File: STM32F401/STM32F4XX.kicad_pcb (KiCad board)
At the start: 2 copper layers, 61 x 68.6 mm, 34 parts, among them J1 DEBUG UART, J2 Conn_02x16_Counter_Clockwise, J3 USB_B_Mini, J4 Conn_02x16_Counter_Clockwise, J5 JTAG SWDIO SWCLK, SW1 ~RESET, U1 STM32F401RCT6, U2 LM1117-3.3, Y1 8MHz

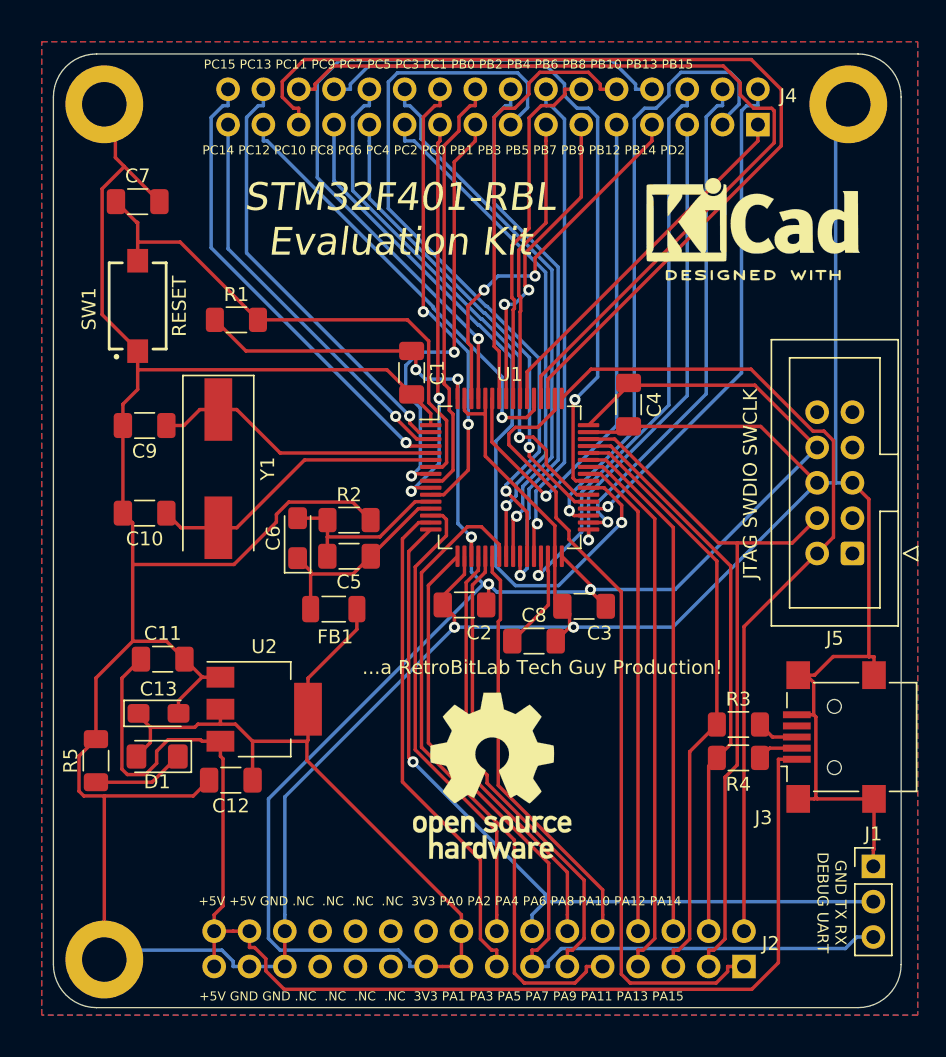
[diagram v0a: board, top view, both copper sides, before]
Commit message: V0.4 USB+ and USB- bug, BOY UART
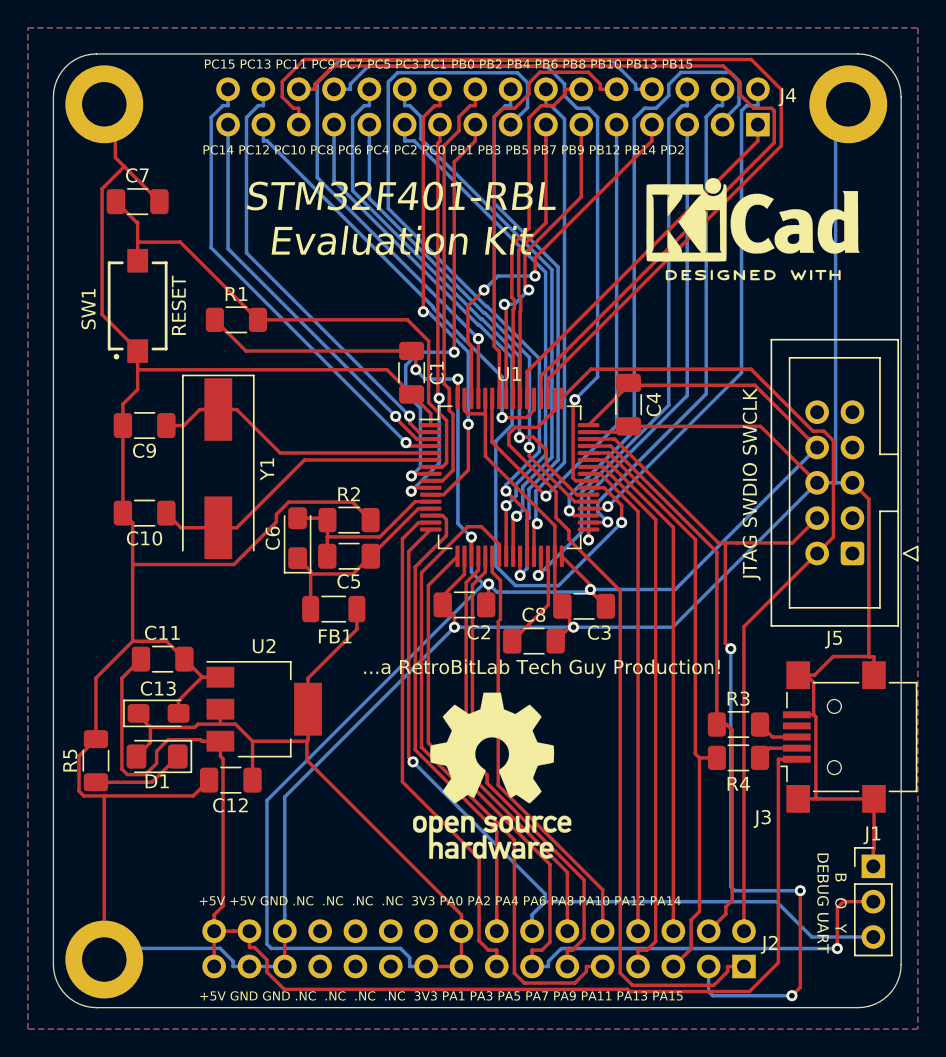
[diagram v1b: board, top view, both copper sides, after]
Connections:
- J1 pad 2: A2 -> A3
- J1 pad 3: A3 -> A2
- R3 pad 1: A11 -> A12
- R4 pad 1: A12 -> A11
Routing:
- net A13: track 51.8 -> 66.0 mm, vias 0 -> 3
- net A3: track 60.3 -> 63.4 mm, vias 0 -> 1
- net A2: track 57.6 -> 58.6 mm
- net +3V3: track 191.0 -> 191.6 mm
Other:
- board text added: "B O Y DEBUG UART"
- board text removed: "GND TX RX DEBUG UART"

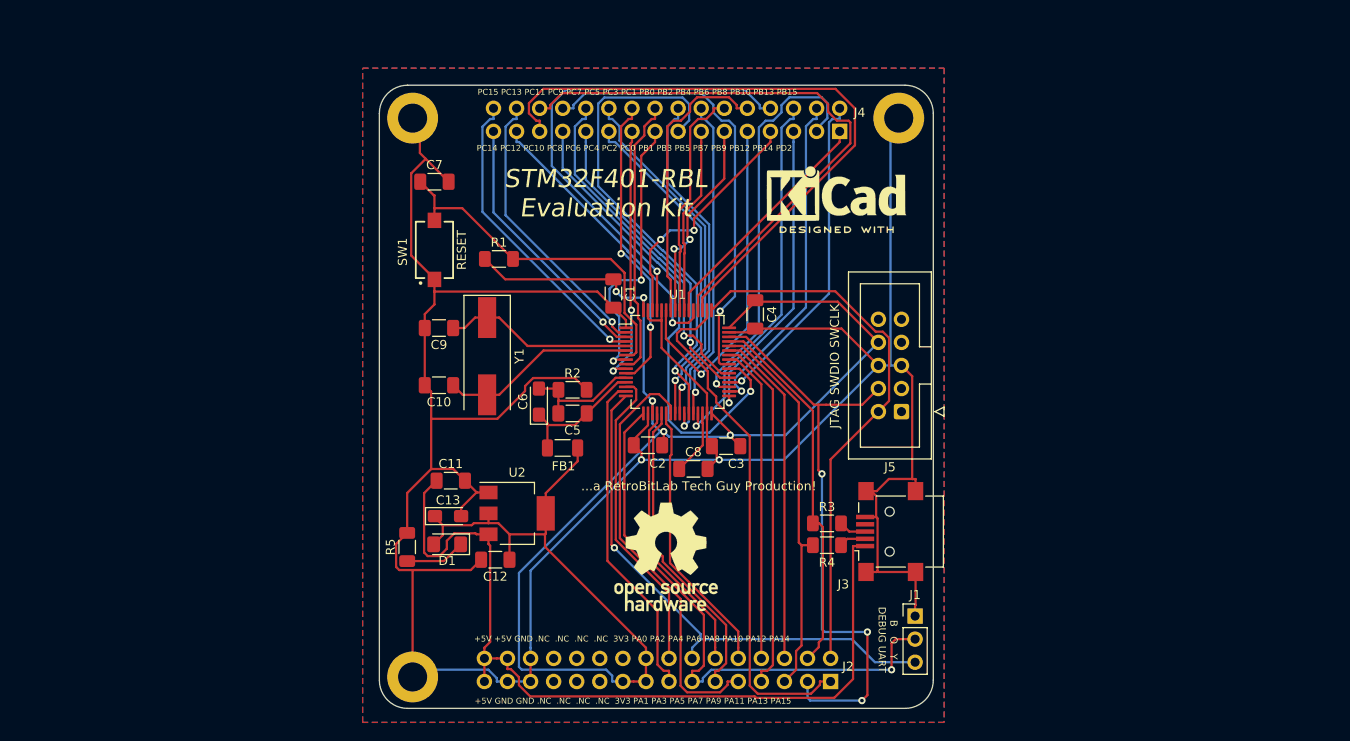
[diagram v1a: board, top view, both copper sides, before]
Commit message: Start transition to a smaller board. Using smallest components footprint
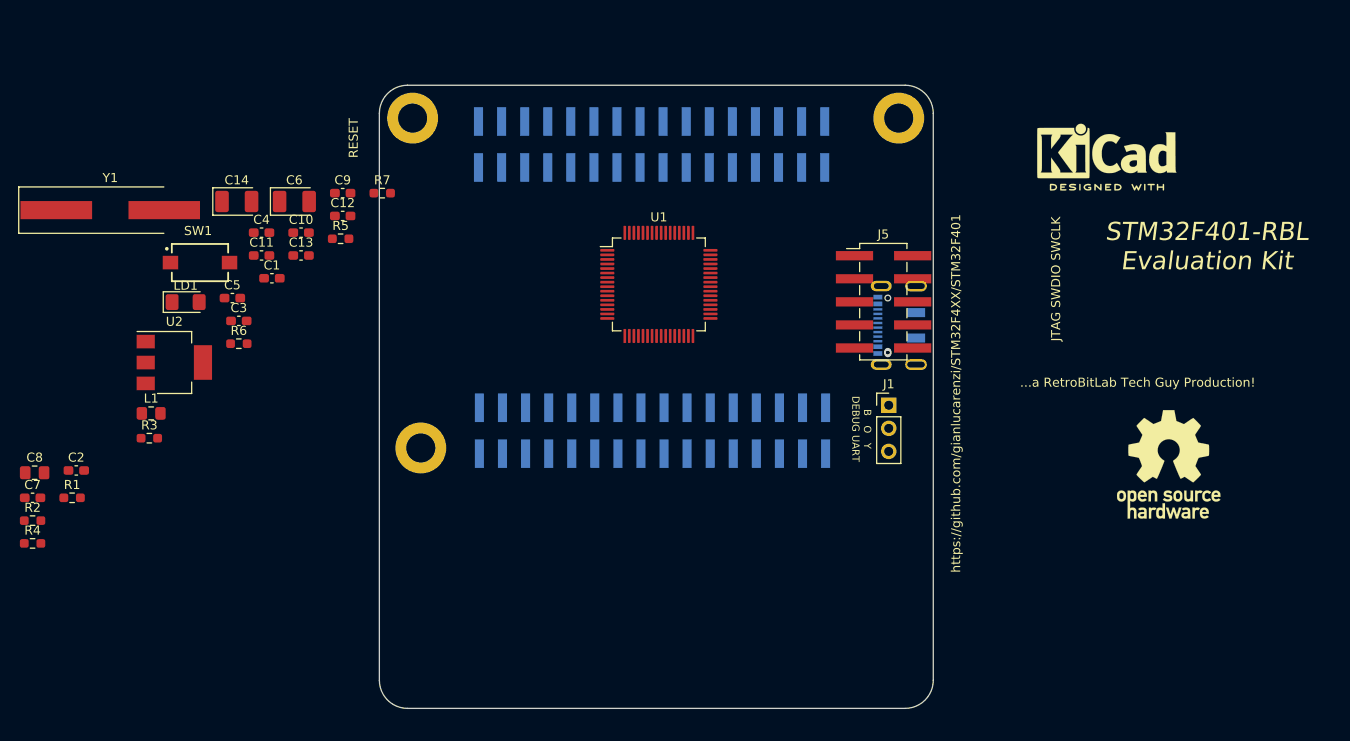
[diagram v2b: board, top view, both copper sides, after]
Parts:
- removed D1: RED, LED_SMD:LED_1206_3216Metric_Pad1.42x1.75mm_HandSolder
- removed FB1: 100uH, Inductor_SMD:L_1206_3216Metric_Pad1.22x1.90mm_HandSolder
- added C14: 10uF, Capacitor_Tantalum_SMD:CP_EIA-3528-12_Kemet-T_Pad1.50x2.35mm_HandSolder, F.Cu at (101.1, 68.7)
- added L1: 90R@100MHZ, Inductor_SMD:L_0805_2012Metric_Pad1.15x1.40mm_HandSolder, F.Cu at (91.7, 92.0)
- added LD1: RED, LED_SMD:LED_1206_3216Metric_Pad1.42x1.75mm_HandSolder, F.Cu at (95.5, 79.7)
- added R6: 5K1, Resistor_SMD:R_0603_1608Metric_Pad0.98x0.95mm_HandSolder, F.Cu at (101.4, 84.3)
- added R7: 330R, Resistor_SMD:R_0603_1608Metric_Pad0.98x0.95mm_HandSolder, F.Cu at (117.2, 67.8)
- C1, C10, C11, C12, C2, C3, C4, C5, C7, C9: footprint Capacitor_SMD:C_1206_3216Metric_Pad1.33x1.80mm_HandSolder -> Capacitor_SMD:C_0603_1608Metric_Pad1.08x0.95mm_HandSolder
- C13: value 10uF -> 100nF; footprint Capacitor_Tantalum_SMD:CP_EIA-3216-12_Kemet-S_Pad1.58x1.35mm_HandSolder -> Capacitor_SMD:C_0603_1608Metric_Pad1.08x0.95mm_HandSolder
- C6: footprint Capacitor_Tantalum_SMD:CP_EIA-3216-12_Kemet-S_Pad1.58x1.35mm_HandSolder -> Capacitor_Tantalum_SMD:CP_EIA-3528-12_Kemet-T_Pad1.50x2.35mm_HandSolder
- C8: footprint Capacitor_SMD:C_1206_3216Metric_Pad1.33x1.80mm_HandSolder -> Capacitor_SMD:C_0805_2012Metric_Pad1.18x1.45mm_HandSolder
- J2, J4: value Conn_02x16_Counter_Clockwise -> CONN_02x16_PIN_SMD_Counter_Clockwise; footprint Connector_PinHeader_2.54mm:PinHeader_2x16_P2.54mm_Vertical -> Connector_PinHeader_2.54mm:PinHeader_2x16_P2.54mm_Vertical_SMD
- J3: value USB_B_Mini -> DX07S016JA1R1500; footprint Connector_USB:USB_Mini-B_Lumberg_2486_01_Horizontal -> RetroBitLab:JAE_DX07S016JA1R1500; moved to B.Cu
- J5: value JTAG SWDIO SWCLK -> CONN_SMD_HEADER_BOX_02x05_Odd_Even_2.54mm; footprint Connector_IDC:IDC-Header_2x05_P2.54mm_Vertical -> RetroBitLab:IDC-Header_2x05_P2.54mm_Vertical_SMD
- R1, R2, R4: footprint Resistor_SMD:R_1206_3216Metric_Pad1.30x1.75mm_HandSolder -> Resistor_SMD:R_0603_1608Metric_Pad0.98x0.95mm_HandSolder
- R3: value 22R -> 5K1; footprint Resistor_SMD:R_1206_3216Metric_Pad1.30x1.75mm_HandSolder -> Resistor_SMD:R_0603_1608Metric_Pad0.98x0.95mm_HandSolder
- R5: value 330R -> 22R; footprint Resistor_SMD:R_1206_3216Metric_Pad1.30x1.75mm_HandSolder -> Resistor_SMD:R_0603_1608Metric_Pad0.98x0.95mm_HandSolder
- U2: value LM1117-3.3 -> AMS1117-3.3
- Y1: value 8MHz -> 8MHzC; footprint Crystal:Crystal_SMD_HC49-SD -> Crystal:Crystal_SMD_HC49-SD_HandSoldering
- moved R4 87.4 mm to (78.7, 106.3)
- moved R3 75.2 mm to (91.5, 94.7)
- moved C8 72.5 mm to (78.9, 98.5)
- moved C2 63.0 mm to (83.5, 98.3), turned to 0 degrees
- moved R2 61.1 mm to (78.7, 103.8)
- moved C7 56.3 mm to (78.7, 101.3)
- moved LOGO1 56.2 mm to (203.7, 97.6)
- moved C3 55.4 mm to (101.4, 81.8), turned to 0 degrees
- moved C4 55.1 mm to (103.9, 72.1), turned to 0 degrees
- moved R1 53.8 mm to (83.0, 101.3)
- moved Y1 44.5 mm to (87.2, 69.6), turned to 0 degrees
- moved C12 41.4 mm to (112.8, 70.3), turned to 0 degrees
- moved U2 41.2 mm to (94.3, 86.4)
- moved C5 39.5 mm to (100.7, 79.3), turned to 0 degrees
- moved C1 37.6 mm to (105.0, 77.1), turned to 0 degrees
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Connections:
- C11 pad 1: VCC -> GND
- C11 pad 2: GND -> Net-(C11-Pad2)
- C12 pad 1: +3V3 -> VCC
- J3 pad 1: VCC -> GND
- J3 pad 2: Net-(J3-Pad2) -> VCC
- J3 pad 5: GND -> /DM
- J3 pad 6: GND -> /DP
- R2 pad 1: /VSSA -> GND
- R2 pad 2: GND -> /VSSA
- R3 pad 1: A12 -> GND
- R4 pad 1: A11 -> A12
- R4 pad 2: Net-(J3-Pad2) -> /DP
- R5 pad 1: Net-(D1-Pad1) -> A11
- R5 pad 2: GND -> /DM
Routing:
- net GND: track 325.6 -> 0.00 mm, vias 2 -> 0
- net +3V3: track 191.6 -> 0.00 mm, vias 5 -> 0
- net VCC: track 94.2 -> 0.00 mm
- net C10: track 70.4 -> 0.00 mm
- net A13: track 66.0 -> 0.00 mm, vias 3 -> 0
- net C11: track 64.6 -> 0.00 mm
- net A3: track 63.4 -> 0.00 mm, vias 1 -> 0
- net A14: track 60.5 -> 0.00 mm
- net A2: track 58.6 -> 0.00 mm, vias 1 -> 0
- net A15: track 57.0 -> 0.00 mm
- net B1: track 54.4 -> 0.00 mm, vias 1 -> 0
- net B8: track 53.3 -> 0.00 mm, vias 1 -> 0
- net C8: track 53.2 -> 0.00 mm, vias 1 -> 0
- net C9: track 49.7 -> 0.00 mm, vias 1 -> 0
- net A7: track 47.2 -> 0.00 mm
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- removed copper zone on B.Cu, net GND
- removed copper zone on F.Cu, net GND

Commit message: V2.0 Smaller
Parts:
- added H4: MountingHole_Pad, MountingHole:MountingHole_3.2mm_M3_DIN965_Pad, F.Cu at (171.0, 95.0)
- added JP1: ~BOOTLOADER, Connector_PinHeader_2.54mm:PinHeader_1x02_P2.54mm_Vertical, F.Cu at (115.4, 76.5)
- added LD2: GREEN, LED_SMD:LED_0805_2012Metric_Pad1.15x1.40mm_HandSolder, F.Cu at (115.7, 83.8)
- added R8: 470R, Resistor_SMD:R_0603_1608Metric_Pad0.98x0.95mm_HandSolder, F.Cu at (115.8, 85.9)
- added R9: 0R, Resistor_SMD:R_0603_1608Metric_Pad0.98x0.95mm_HandSolder, F.Cu at (120.1, 85.6)
- J2, J4: value CONN_02x16_PIN_SMD_Counter_Clockwise -> CONN_02x16_PIN_SMD_Odd_Even_2.54mm
- J3: moved to F.Cu
- LOGO2, R3, R6, U1: moved to B.Cu
- Y1: footprint Crystal:Crystal_SMD_HC49-SD_HandSoldering -> Crystal:Crystal_SMD_HC49-SD
- moved R4 91.9 mm to (163.5, 70.9)
- moved R3 75.3 mm to (163.5, 72.5)
- moved LOGO2 72.5 mm to (126.6, 81.0), turned to 180 degrees
- moved LOGO1 69.3 mm to (135.5, 85.4)
- moved C8 67.7 mm to (137.1, 63.9), turned to 225 degrees
- moved C2 66.4 mm to (140.0, 63.5), turned to 225 degrees
- moved C11 65.6 mm to (168.8, 65.2)
- moved U2 64.3 mm to (157.6, 75.3), turned to 90 degrees
- moved R6 63.6 mm to (163.5, 70.9), turned to 180 degrees
- moved R2 60.1 mm to (133.1, 78.3)
- moved C14 57.1 mm to (158.2, 68.9)
- moved Y1 55.7 mm to (142.8, 73.1), turned to 135 degrees
- moved C3 52.9 mm to (152.4, 68.0), turned to 135 degrees
- moved C12 51.3 mm to (163.7, 77.1)
- moved R5 50.9 mm to (163.5, 72.5)
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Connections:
- J2 pad 1: A15 -> GND
- J2 pad 10: A6 -> Net-(J2-Pad10)
- J2 pad 11: A5 -> C10
- J2 pad 12: A4 -> A15
- J2 pad 13: A3 -> C12
- J2 pad 14: A2 -> C11
- J2 pad 15: A1 -> B3
- J2 pad 16: A0 -> D2
- J2 pad 17: +3V3 -> B5
- J2 pad 18: +3V3 -> B4
- J2 pad 19: +3V3 -> B7
- J2 pad 2: A14 -> GND
- J2 pad 20: Net-(J2-Pad20) -> B6
- J2 pad 21: Net-(J2-Pad21) -> B9
- J2 pad 22: Net-(J2-Pad22) -> B8
- J2 pad 23: Net-(J2-Pad23) -> C14
- J2 pad 24: Net-(J2-Pad24) -> C13
- J2 pad 25: Net-(J2-Pad25) -> C0
- J2 pad 26: Net-(J2-Pad26) -> C15
- J2 pad 27: GND -> C2
- J2 pad 28: GND -> C1
- J2 pad 29: GND -> A0
- J2 pad 3: A13 -> GND
- J2 pad 30: VCC -> C3
- J2 pad 31: VCC -> A2
- J2 pad 32: VCC -> A1
- J2 pad 4: A12 -> GND
- J2 pad 5: A11 -> +3V3
- J2 pad 6: A10 -> VCC
- J2 pad 7: A9 -> +3V3
- J2 pad 8: A8 -> VCC
- J2 pad 9: A7 -> A14
- J4 pad 1: D2 -> A13
- J4 pad 10: B6 -> C6
- J4 pad 11: B5 -> B15
- J4 pad 12: B4 -> B14
- J4 pad 13: B3 -> B13
- J4 pad 14: B2 -> B12
- J4 pad 15: B1 -> B10
- J4 pad 16: B0 -> B2
- J4 pad 17: C0 -> B1
- J4 pad 18: C1 -> B0
- J4 pad 19: C2 -> C5
- J4 pad 2: B15 -> A12
- J4 pad 20: C3 -> C4
- J4 pad 21: C4 -> A7
- J4 pad 22: C5 -> A6
- J4 pad 23: C6 -> A5
- J4 pad 24: C7 -> A4
- J4 pad 25: C8 -> A3
- J4 pad 26: C9 -> +3V3
- J4 pad 27: C10 -> VCC
- J4 pad 28: C11 -> +3V3
- J4 pad 29: C12 -> GND
- J4 pad 3: B14 -> A11
- J4 pad 30: C13 -> GND
- J4 pad 31: C14 -> GND
- J4 pad 32: C15 -> GND
- J4 pad 4: B13 -> A10
- J4 pad 5: B12 -> A9
- J4 pad 6: B10 -> A8
- J4 pad 7: B9 -> C9
- J4 pad 8: B8 -> C8
- J4 pad 9: B7 -> C7
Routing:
- net GND: track 0.00 -> 273.7 mm, vias 0 -> 28
- net +3V3: track 0.00 -> 245.9 mm, vias 0 -> 33
- net VCC: track 0.00 -> 120.6 mm, vias 0 -> 4
- net A3: track 0.00 -> 93.3 mm, vias 0 -> 3
- net A2: track 0.00 -> 83.3 mm
- net C11: track 0.00 -> 72.4 mm, vias 0 -> 2
- net A0: track 0.00 -> 48.2 mm, vias 0 -> 1
- net A14: track 0.00 -> 43.1 mm, vias 0 -> 2
- net A5: track 0.00 -> 40.9 mm
- net C1: track 0.00 -> 40.0 mm, vias 0 -> 2
- net A12: track 0.00 -> 37.7 mm, vias 0 -> 1
- net A13: track 0.00 -> 37.4 mm, vias 0 -> 1
- net Net-(C7-Pad1): track 0.00 -> 35.9 mm, vias 0 -> 1
- net A11: track 0.00 -> 30.6 mm, vias 0 -> 1
- net C10: track 0.00 -> 30.2 mm
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- added copper zone on F.Cu, net +3V3
- added copper zone on B.Cu, net GND
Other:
- board size 61 x 68.6 mm -> 63 x 49.2 mm
- rule pad_to_mask_clearance: 0 -> 0.1
- board text added: "STLink V2 PROGRAMMER"
- board text added: "STM32F401-RBL Evaluation Kit V2"
- board text removed: "+5V +5V GND .NC .NC .NC .NC 3V3 PA0 PA2 PA4 PA6 PA8 PA10 PA12 PA14"
- board text removed: "+5V GND GND .NC .NC .NC .NC 3V3 PA1 PA3 PA5 PA7 PA9 PA11 PA13 PA15"
- board text removed: "JTAG SWDIO SWCLK"
- board text removed: "PC14 PC12 PC10 PC8 PC6 PC4 PC2 PC0 PB1 PB3 PB5 PB7 PB9 PB12 PB14 PD2"
- board text removed: "PC15 PC13 PC11 PC9 PC7 PC5 PC3 PC1 PB0 PB2 PB4 PB6 PB8 PB10 PB13 PB15"
- board text removed: "STM32F401-RBL Evaluation Kit"
